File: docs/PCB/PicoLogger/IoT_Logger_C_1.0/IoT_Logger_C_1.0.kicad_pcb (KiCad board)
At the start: 2 copper layers, 94.7 x 71.8 mm, 93 parts, among them J1 AVR-ISP-10, J2 ESP_UART, J3 USB-C, J4 Sensor, J5 LCD 16x2, J6 SPI, J7 CON, Q1 BSS138, Q2 BC817-40-DIO, SW1 Tact Switch 6x6mm / 13mm, SW2 Tact Switch 6x6mm / 13mm, SW3 Tact Switch 6x6mm / 13mm, SW4 Tact Switch 6x6mm / 13mm, U1 ATmega328PB-A, U2 ESP32-C6-WROOM-1U, U3 AP63200WU, U4 PCA9306DCUR, U5 TPD2EUSB30, Y1 16.00M-SMDXT324

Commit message: Code added, documentation review.
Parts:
- added Q3: BSS138, Package_TO_SOT_SMD:SOT-23, F.Cu at (106.3, 105.0)
- added R29: 100kR, Resistor_SMD:R_0603_1608Metric, F.Cu at (111.0, 82.7)
- added R30: 4k7R, Resistor_SMD:R_0603_1608Metric, F.Cu at (111.0, 84.3)
- added R31: 1k, Resistor_SMD:R_0603_1608Metric, F.Cu at (112.2, 104.9)
- added R32: 100k, Resistor_SMD:R_0603_1608Metric, F.Cu at (109.4, 105.0)
- C1, C2, C3, C4, C5, C6, C7, C8: footprint Capacitor_SMD:C_0805_2012Metric_Pad1.18x1.45mm_HandSolder -> Capacitor_SMD:C_0603_1608Metric
- L1: footprint Inductor_SMD:L_0805_2012Metric_Pad1.05x1.20mm_HandSolder -> Inductor_SMD:L_0603_1608Metric
- R1: footprint Resistor_SMD:R_0805_2012Metric -> Resistor_SMD:R_0603_1608Metric
- moved C7 23.5 mm to (112.6, 109.9), turned to 0 degrees
- moved R17 1.90 mm to (98.1, 74.8)
- moved R18 1.90 mm to (93.3, 74.8)
- moved U5 1.30 mm to (95.5, 74.6)
- moved TP1 0.60 mm to (115.5, 78.2)
- moved R1 0.57 mm to (136.3, 120.1)
- moved J3 0.55 mm to (98.5, 71.3)
- moved R6 0.55 mm to (117.0, 83.2)
- moved R7 0.55 mm to (116.9, 81.4)
- moved R5 0.43 mm to (114.6, 75.0)
- moved C9 0.42 mm to (114.6, 73.3)
- moved C25 0.40 mm to (88.5, 68.1)
- moved C1 0.38 mm to (122.5, 110.2)
- moved Q2 0.37 mm to (109.5, 99.8)
- moved R16 0.37 mm to (108.9, 97.2)
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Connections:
- U2 pad 9: unconnected-(U2-GPIO1/ADC1_CH1/XTAL_32K_N-Pad9) -> GPIO1
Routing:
- net EN: track 68.6 -> 108.3 mm, vias 1 -> 2
- net PD7: track 0.00 -> 35.9 mm, vias 0 -> 2
- net PC3: track 0.00 -> 29.9 mm
- net GPIO1: track 0.00 -> 23.1 mm
- net PE3: track 38.7 -> 48.5 mm, vias 2 -> 4
- net Net-(Q3-G): track 0.00 -> 4.51 mm
- net RESET_CON: track 108.8 -> 112.6 mm
- net +5V: track 281.6 -> 278.2 mm, vias 10 -> 9
- net USB_VBUS: track 23.9 -> 26.7 mm
- net USB_D-: track 33.2 -> 30.6 mm
- net USB_D+: track 34.1 -> 32.1 mm, vias 2 -> 0
- net USB_CC2: track 15.2 -> 13.5 mm
- net USB_CC1: track 4.59 -> 3.17 mm
- net GPIO19: track 45.9 -> 44.7 mm
- net TXD0: track 61.8 -> 62.7 mm
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
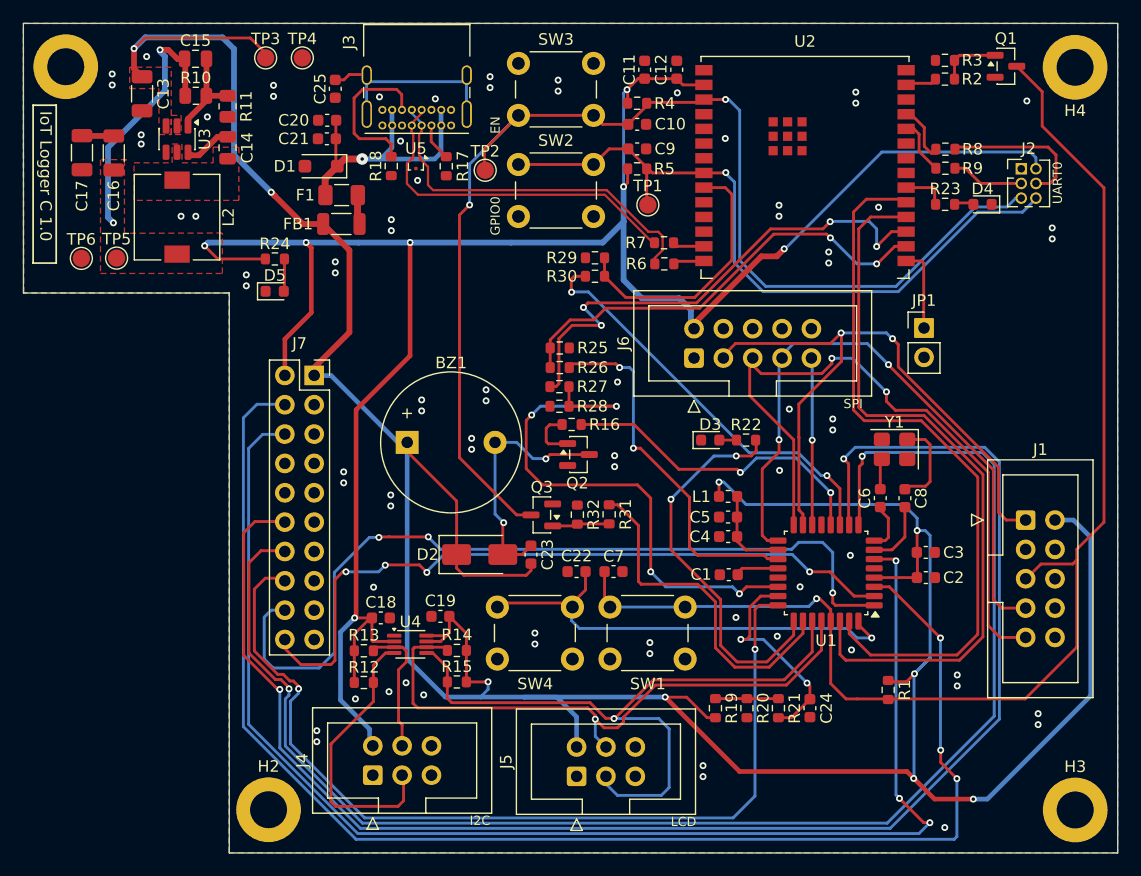
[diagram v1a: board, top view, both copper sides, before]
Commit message: New logger revisions added.
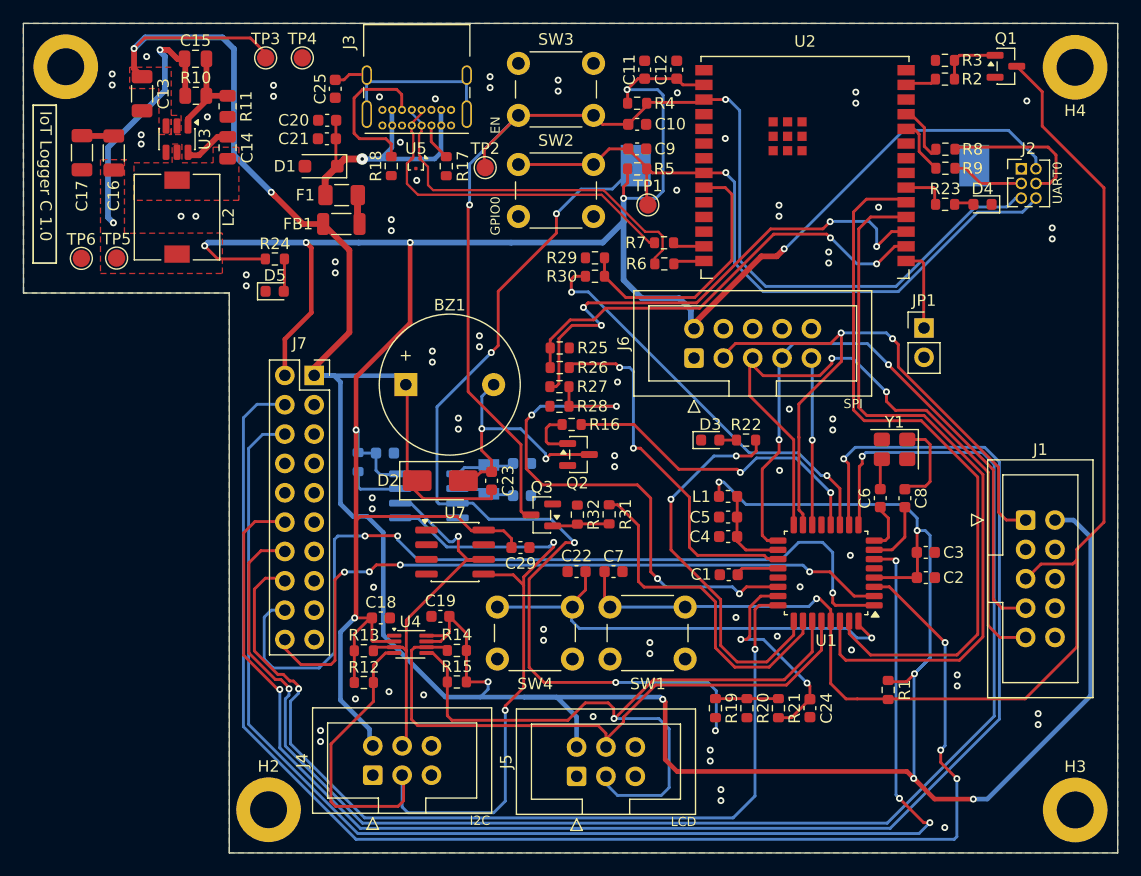
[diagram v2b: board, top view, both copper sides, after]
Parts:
- added BT1: CR2032, Battery:BatteryHolder_Keystone_1060_1x2032, B.Cu at (129.1, 74.8)
- added C26: 100nF, Capacitor_SMD:C_0603_1608Metric, B.Cu at (92.8, 99.6)
- added C27: 12pF, Capacitor_SMD:C_0603_1608Metric, B.Cu at (104.6, 100.5)
- added C28: 12pF, Capacitor_SMD:C_0603_1608Metric, B.Cu at (104.6, 103.3)
- added C29: 100nF, Capacitor_SMD:C_0603_1608Metric, F.Cu at (104.5, 107.8)
- added R33: 4k7R, Resistor_SMD:R_0603_1608Metric, B.Cu at (90.5, 100.4)
- added U6: MCP7940N-xSN, Package_SO:SOIC-8_3.9x4.9mm_P1.27mm, B.Cu at (96.6, 103.3)
- added U7: FM24CL16B, Package_SO:SOIC-8_3.9x4.9mm_P1.27mm, F.Cu at (98.8, 108.2)
- added Y2: QT3CD-32.768KEZY-T, Crystal:Crystal_SMD_3215-2Pin_3.2x1.5mm, B.Cu at (101.8, 101.9)
- R12, R13: value 0 -> 4k7R
- R14, R15: value 4K7 -> 4k7R
- R16: value 1K -> 1kR
- R17, R18: value 5K1 -> 5k1R
- R19: value 200k -> 200kR
- R2, R31: value 1k -> 1kR
- R20: value 68k -> 68kR
- R3, R32: value 100k -> 100kR
- R4, R5: value 10k -> 10kR
- moved C23 7.25 mm to (102.0, 102.0)
- moved D2 7.25 mm to (97.6, 102.0)
- moved BZ1 5.00 mm to (94.6, 93.7)
- moved TP2 0.23 mm to (101.5, 74.9)
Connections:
- R19 pad 1: +5V -> +BAT
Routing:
- net +BAT: track 0.00 -> 84.9 mm, vias 0 -> 5
- net I2C_SDA_3V3: track 24.0 -> 78.7 mm, vias 0 -> 2
- net +3.3V: track 209.7 -> 240.6 mm, vias 9 -> 10
- net I2C_SCL_3V3: track 12.4 -> 33.9 mm, vias 0 -> 1
- net Net-(U6-X2): track 0.00 -> 5.14 mm
- net Net-(U6-X1): track 0.00 -> 5.11 mm
- net GPIOB5: track 0.00 -> 5.06 mm
- net +5V: track 278.2 -> 283.0 mm
- net SDA0: track 59.4 -> 62.0 mm
- net OC2B: track 73.1 -> 75.7 mm
- net PD4: track 62.5 -> 61.2 mm
- net EN: track 108.3 -> 107.3 mm
- net SCL0: track 52.6 -> 53.1 mm, vias 1 -> 0
- net GND: vias 76 -> 77
